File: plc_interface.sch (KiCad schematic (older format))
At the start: 19 parts, among them J501 GPIO, Q601 AO3400A, Q602 AO3401A, U502 PLC_Stamp_mini_2, U601 AMS1117-3.3

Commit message: Add files via upload
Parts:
- removed J501: GPIO, symbol Connector_Generic:Conn_01x04
- added J601: GPIO, Connector_PinSocket_2.54mm:PinSocket_1x06_P2.54mm_Vertical, symbol Connector_Generic:Conn_01x06
- C601, C602: footprint (none) -> Capacitor_SMD:C_0402_1005Metric
- D501, D602: footprint (none) -> LED_SMD:LED_0805_2012Metric
- Q601: footprint (none) -> Package_TO_SOT_SMD:SOT-23
- R501, R502, R503, R504, R505, R508, R510, R606, R607, R609: footprint (none) -> Resistor_SMD:R_0402_1005Metric
- U502: footprint (none) -> PLC stamp:PLC_Stamp_mini_2
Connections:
- wire segments 90 -> 92
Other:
- note added: "Boot Source: Flash"
- note added: "Host Interface: SPI Slave"
- note added: "SPI Slave Mode: Lagacy"
- moved on the sheet: C601, C602, D601, D602, Q601, Q602, R601, R602, R603, R604, R605, R606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

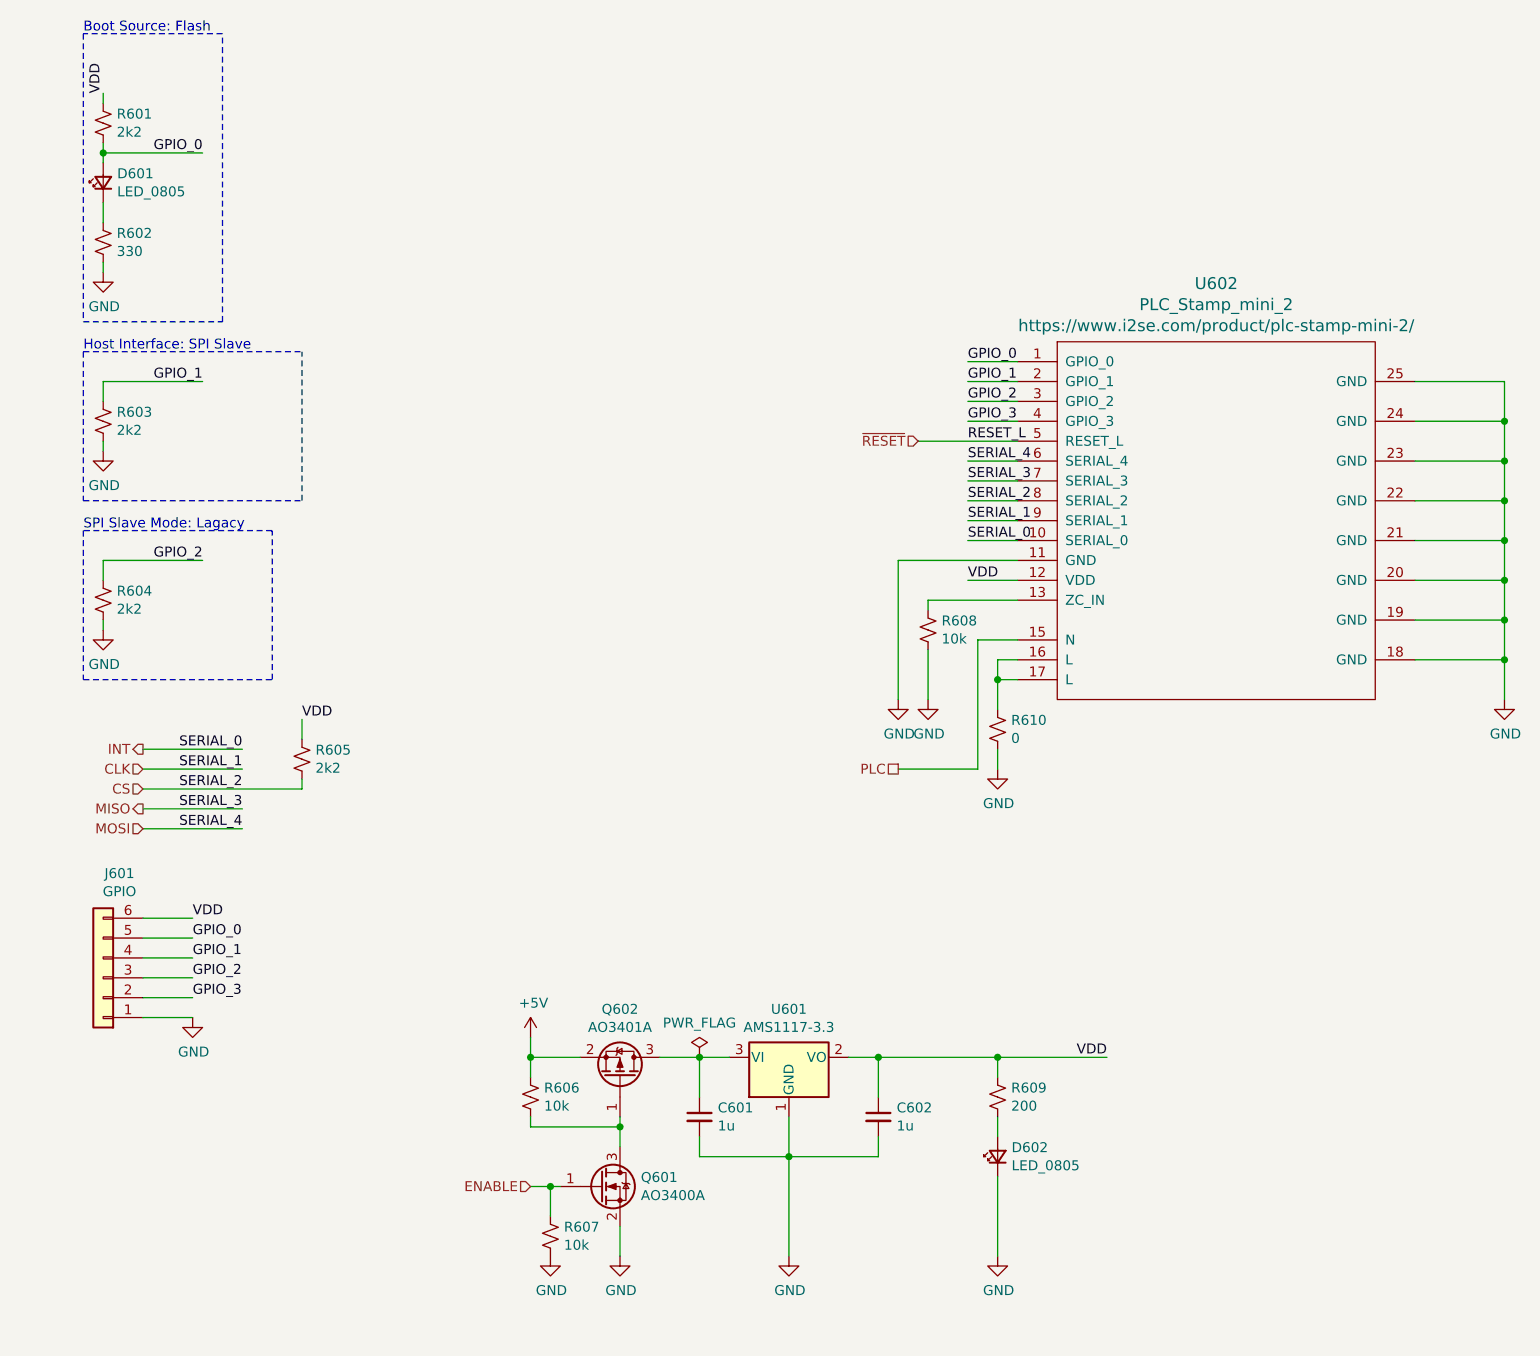
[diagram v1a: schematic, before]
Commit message: Submited for production & smt assembly
v0.01
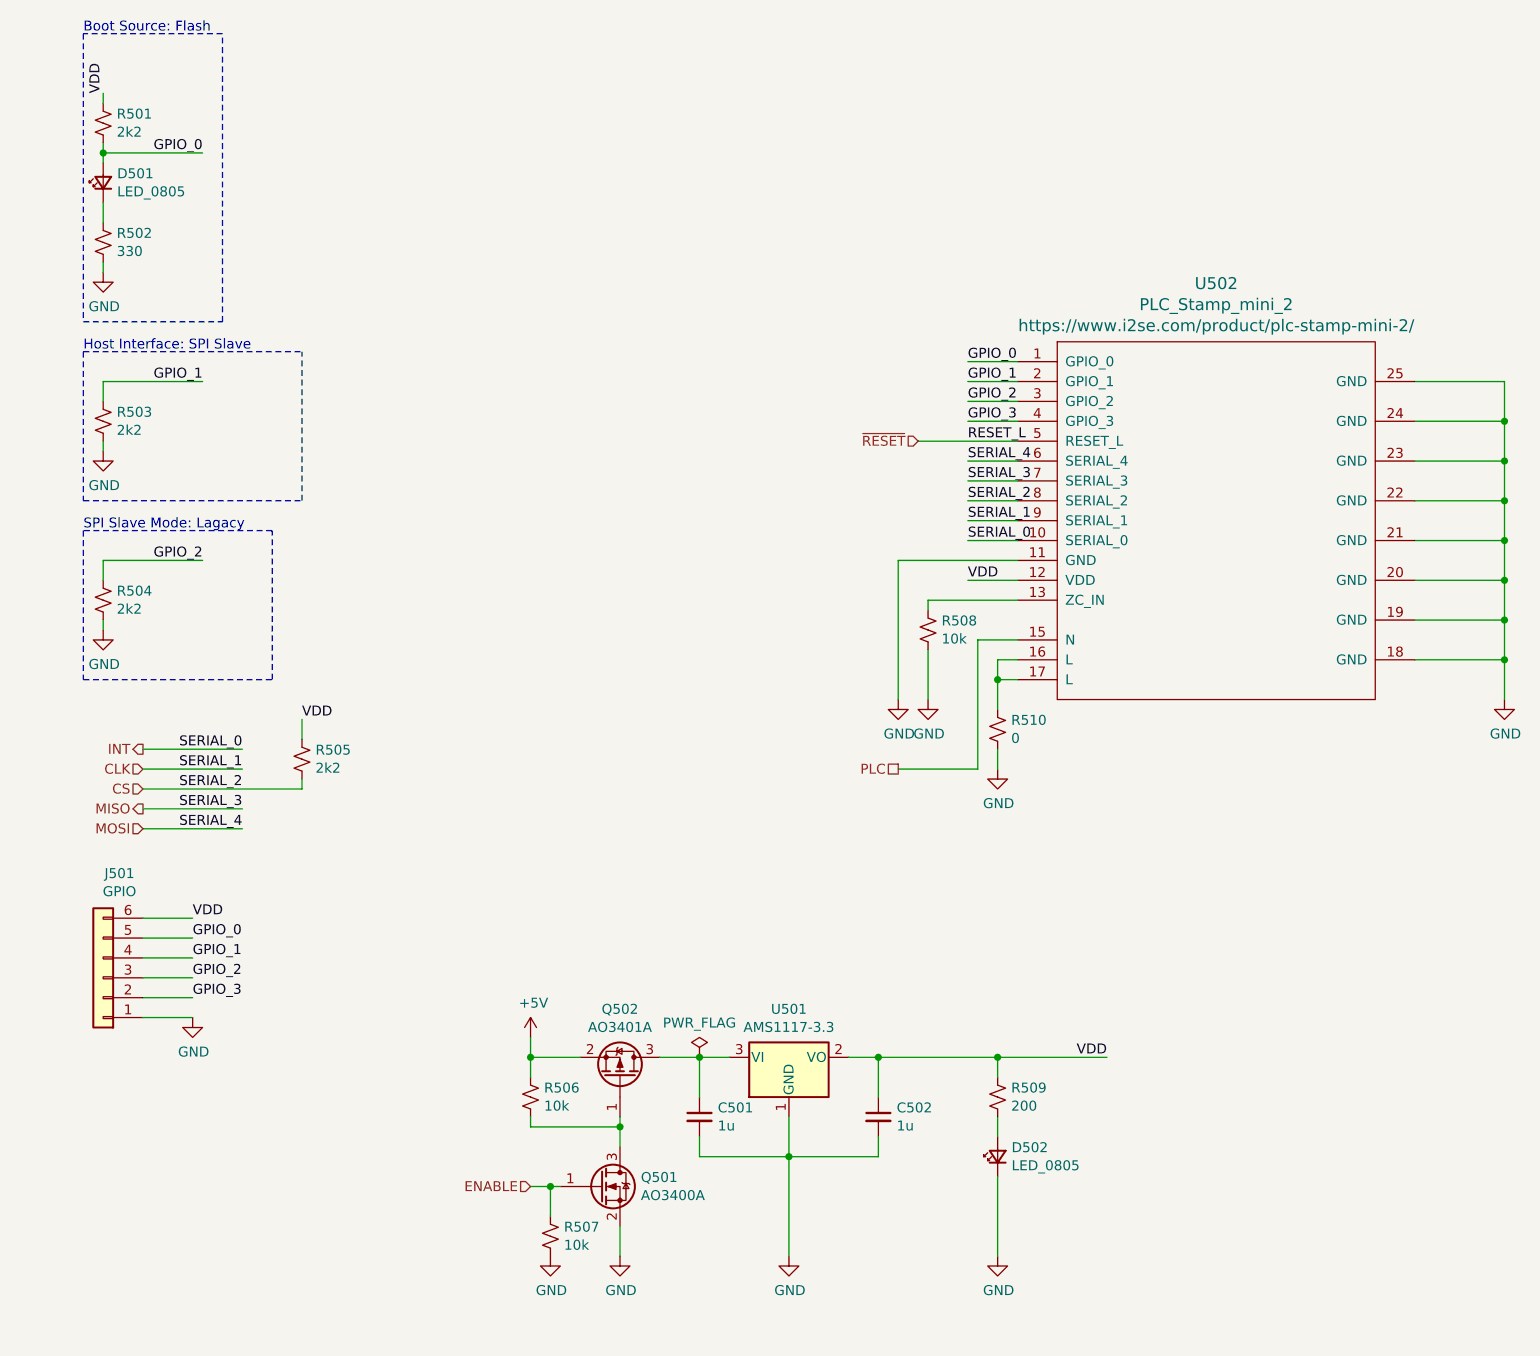
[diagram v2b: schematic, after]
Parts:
- J601: footprint Connector_PinSocket_2.54mm:PinSocket_1x06_P2.54mm_Vertical -> Connector_PinHeader_2.54mm:PinHeader_1x06_P2.54mm_Vertical
- R510: footprint Resistor_SMD:R_0402_1005Metric -> Resistor_SMD:R_0805_2012Metric
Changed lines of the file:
@@
 $Descr A4 11693 8268
 encoding utf-8
-Sheet 6 10
+Sheet 4 10
 Title ""
 Date ""
@@
 AR Path="/5EF2D1B7/5EF2D3AC" Ref="U502"  Part="1"
 AR Path="/5F84D431/5EF2D3AC" Ref="U602"  Part="1"
-F 0 "U602" H 6300 4243 60  0000 C CNN
+F 0 "U502" H 6300 4243 60  0000 C CNN
 F 1 "PLC_Stamp_mini_2" H 6300 4137 60  0000 C CNN
 F 2 "PLC stamp:PLC_Stamp_mini_2" H 6300 3150 60  0001 C CNN
@@
 AR Path="/5EF2D1B7/5EF2EA16" Ref="#PWR0512"  Part="1"
 AR Path="/5F84D431/5EF2EA16" Ref="#PWR0612"  Part="1"
-F 0 "#PWR0612" H 7750 3700 50  0001 C CNN
+F 0 "#PWR0512" H 7750 3700 50  0001 C CNN
 F 1 "GND" H 7755 3777 50  0000 C CNN
 F 2 "" H 7750 3950 50  0001 C CNN
@@
 AR Path="/5EF2D1B7/5EF2FAF1" Ref="R508"  Part="1"
 AR Path="/5F84D431/5EF2FAF1" Ref="R608"  Part="1"
-F 0 "R608" H 4918 3646 50  0000 L CNN
+F 0 "R508" H 4918 3646 50  0000 L CNN
 F 1 "10k" H 4918 3555 50  0000 L CNN
 F 2 "Resistor_SMD:R_0402_1005Metric" H 4850 3600 50  0001 C CNN
@@
 AR Path="/5EF2D1B7/5EF3018B" Ref="#PWR0508"  Part="1"
 AR Path="/5F84D431/5EF3018B" Ref="#PWR0608"  Part="1"
-F 0 "#PWR0608" H 4850 3700 50  0001 C CNN
+F 0 "#PWR0508" H 4850 3700 50  0001 C CNN
 F 1 "GND" H 4855 3777 50  0000 C CNN
 F 2 "" H 4850 3950 50  0001 C CNN
@@
 AR Path="/5EF2D1B7/5EF309BC" Ref="#PWR0507"  Part="1"
 AR Path="/5F84D431/5EF309BC" Ref="#PWR0607"  Part="1"
-F 0 "#PWR0607" H 4700 3700 50  0001 C CNN
+F 0 "#PWR0507" H 4700 3700 50  0001 C CNN
 F 1 "GND" H 4705 3777 50  0000 C CNN
 F 2 "" H 4700 3950 50  0001 C CNN
@@
 AR Path="/5EF2D1B7/5EF3506C" Ref="R501"  Part="1"
 AR Path="/5F84D431/5EF3506C" Ref="R601"  Part="1"
-F 0 "R601" H 768 1096 50  0000 L CNN
+F 0 "R501" H 768 1096 50  0000 L CNN
 F 1 "2k2" H 768 1005 50  0000 L CNN
 F 2 "Resistor_SMD:R_0402_1005Metric" H 700 1050 50  0001 C CNN
@@
 AR Path="/5EF2D1B7/5EF38FDC" Ref="R503"  Part="1"
 AR Path="/5F84D431/5EF38FDC" Ref="R603"  Part="1"
-F 0 "R603" H 768 2596 50  0000 L CNN
+F 0 "R503" H 768 2596 50  0000 L CNN
 F 1 "2k2" H 768 2505 50  0000 L CNN
 F 2 "Resistor_SMD:R_0402_1005Metric" H 700 2550 50  0001 C CNN
@@
 AR Path="/5EF2D1B7/5EF3A4A8" Ref="#PWR0502"  Part="1"
 AR Path="/5F84D431/5EF3A4A8" Ref="#PWR0602"  Part="1"
-F 0 "#PWR0602" H 700 2450 50  0001 C CNN
+F 0 "#PWR0502" H 700 2450 50  0001 C CNN
 F 1 "GND" H 705 2527 50  0000 C CNN
 F 2 "" H 700 2700 50  0001 C CNN
@@
 AR Path="/5EF2D1B7/5EF419EA" Ref="R504"  Part="1"
 AR Path="/5F84D431/5EF419EA" Ref="R604"  Part="1"
-F 0 "R604" H 768 3496 50  0000 L CNN
+F 0 "R504" H 768 3496 50  0000 L CNN
 F 1 "2k2" H 768 3405 50  0000 L CNN
 F 2 "Resistor_SMD:R_0402_1005Metric" H 700 3450 50  0001 C CNN
@@
 AR Path="/5EF2D1B7/5EF41CF1" Ref="#PWR0503"  Part="1"
 AR Path="/5F84D431/5EF41CF1" Ref="#PWR0603"  Part="1"
-F 0 "#PWR0603" H 700 3350 50  0001 C CNN
+F 0 "#PWR0503" H 700 3350 50  0001 C CNN
 F 1 "GND" H 705 3427 50  0000 C CNN
 F 2 "" H 700 3600 50  0001 C CNN
@@
 AR Path="/5EF2D1B7/5EF4D79D" Ref="D501"  Part="1"
 AR Path="/5F84D431/5EF4D79D" Ref="D601"  Part="1"
-F 0 "D601" V 746 1280 50  0000 R CNN
+F 0 "D501" V 746 1280 50  0000 R CNN
 F 1 "LED_0805" V 655 1280 50  0000 R CNN
 F 2 "LED_SMD:LED_0805_2012Metric" V 700 1350 50  0001 C CNN
@@
 AR Path="/5EF2D1B7/5EF4E287" Ref="R502"  Part="1"
 AR Path="/5F84D431/5EF4E287" Ref="R602"  Part="1"
-F 0 "R602" H 768 1696 50  0000 L CNN
+F 0 "R502" H 768 1696 50  0000 L CNN
 F 1 "330" H 768 1605 50  0000 L CNN
 F 2 "Resistor_SMD:R_0402_1005Metric" H 700 1650 50  0001 C CNN
@@
 AR Path="/5EF2D1B7/5EF4E68F" Ref="#PWR0501"  Part="1"
 AR Path="/5F84D431/5EF4E68F" Ref="#PWR0601"  Part="1"
-F 0 "#PWR0601" H 700 1550 50  0001 C CNN
+F 0 "#PWR0501" H 700 1550 50  0001 C CNN
 F 1 "GND" H 705 1627 50  0000 C CNN
 F 2 "" H 700 1800 50  0001 C CNN
@@
 AR Path="/5EF2D1B7/5EF64DDA" Ref="#PWR0509"  Part="1"
 AR Path="/5F84D431/5EF64DDA" Ref="#PWR0609"  Part="1"
-F 0 "#PWR0609" H 5200 4050 50  0001 C CNN
+F 0 "#PWR0509" H 5200 4050 50  0001 C CNN
 F 1 "GND" H 5205 4127 50  0000 C CNN
 F 2 "" H 5200 4300 50  0001 C CNN
@@
 AR Path="/5F84D431/5F90AF35" Ref="U601"  Part="1"
 AR Path="/5EF2D1B7/5F90AF35" Ref="U501"  Part="1"
-F 0 "U601" H 4150 5992 50  0000 C CNN
+F 0 "U501" H 4150 5992 50  0000 C CNN
 F 1 "AMS1117-3.3" H 4150 5901 50  0000 C CNN
 F 2 "Package_TO_SOT_SMD:SOT-223-3_TabPin2" H 4150 5950 50  0001 C CNN
@@
 AR Path="/5F84D431/5F90C7F9" Ref="C601"  Part="1"
 AR Path="/5EF2D1B7/5F90C7F9" Ref="C501"  Part="1"
-F 0 "C601" H 3792 6096 50  0000 L CNN
+F 0 "C501" H 3792 6096 50  0000 L CNN
 F 1 "1u" H 3792 6005 50  0000 L CNN
 F 2 "Capacitor_SMD:C_0402_1005Metric" H 3700 6050 50  0001 C CNN
@@
 AR Path="/5F84D431/5F90CBCB" Ref="C602"  Part="1"
 AR Path="/5EF2D1B7/5F90CBCB" Ref="C502"  Part="1"
-F 0 "C602" H 4692 6096 50  0000 L CNN
+F 0 "C502" H 4692 6096 50  0000 L CNN
 F 1 "1u" H 4692 6005 50  0000 L CNN
 F 2 "Capacitor_SMD:C_0402_1005Metric" H 4600 6050 50  0001 C CNN
@@
 AR Path="/5F84D431/5F90D006" Ref="R609"  Part="1"
 AR Path="/5EF2D1B7/5F90D006" Ref="R509"  Part="1"
-F 0 "R609" H 5268 5996 50  0000 L CNN
+F 0 "R509" H 5268 5996 50  0000 L CNN
 F 1 "200" H 5268 5905 50  0000 L CNN
 F 2 "Resistor_SMD:R_0402_1005Metric" H 5200 5950 50  0001 C CNN
@@
 AR Path="/5F84D431/5F90D610" Ref="D602"  Part="1"
 AR Path="/5EF2D1B7/5F90D610" Ref="D502"  Part="1"
-F 0 "D602" V 5246 6180 50  0000 R CNN
+F 0 "D502" V 5246 6180 50  0000 R CNN
 F 1 "LED_0805" V 5155 6180 50  0000 R CNN
 F 2 "LED_SMD:LED_0805_2012Metric" V 5200 6250 50  0001 C CNN
@@
 AR Path="/5F84D431/5EECEA59" Ref="Q602"  Part="1"
 AR Path="/5EF2D1B7/5EECEA59" Ref="Q502"  Part="1"
-F 0 "Q602" V 3642 5850 50  0000 C CNN
+F 0 "Q502" V 3642 5850 50  0000 C CNN
 F 1 "AO3401A" V 3551 5850 50  0000 C CNN
 F 2 "Package_TO_SOT_SMD:SOT-23" H 3500 5775 50  0001 L CIN
@@
 AR Path="/5F84D431/5EED0EB8" Ref="#PWR0604"  Part="1"
 AR Path="/5EF2D1B7/5EED0EB8" Ref="#PWR0504"  Part="1"
-F 0 "#PWR0604" H 2850 5500 50  0001 C CNN
+F 0 "#PWR0504" H 2850 5500 50  0001 C CNN
 F 1 "+5V" H 2865 5823 50  0000 C CNN
 F 2 "" H 2850 5650 50  0001 C CNN
@@
 AR Path="/5F84D431/5EED1407" Ref="R606"  Part="1"
 AR Path="/5EF2D1B7/5EED1407" Ref="R506"  Part="1"
-F 0 "R606" H 2918 5996 50  0000 L CNN
+F 0 "R506" H 2918 5996 50  0000 L CNN
 F 1 "10k" H 2918 5905 50  0000 L CNN
 F 2 "Resistor_SMD:R_0402_1005Metric" H 2850 5950 50  0001 C CNN
@@
 AR Path="/5F84D431/5EEE7A70" Ref="Q601"  Part="1"
 AR Path="/5EF2D1B7/5EEE7A70" Ref="Q501"  Part="1"
-F 0 "Q601" H 3405 6446 50  0000 L CNN
+F 0 "Q501" H 3405 6446 50  0000 L CNN
 F 1 "AO3400A" H 3405 6355 50  0000 L CNN
 F 2 "Package_TO_SOT_SMD:SOT-23" H 3400 6500 50  0001 C CNN
@@
 AR Path="/5F84D431/5EEE8A1F" Ref="R607"  Part="1"
 AR Path="/5EF2D1B7/5EEE8A1F" Ref="R507"  Part="1"
-F 0 "R607" H 3018 6696 50  0000 L CNN
+F 0 "R507" H 3018 6696 50  0000 L CNN
 F 1 "10k" H 3018 6605 50  0000 L CNN
 F 2 "Resistor_SMD:R_0402_1005Metric" H 2950 6650 50  0001 C CNN
@@
 AR Path="/5F84D431/5EEFA299" Ref="#PWR0605"  Part="1"
 AR Path="/5EF2D1B7/5EEFA299" Ref="#PWR0505"  Part="1"
-F 0 "#PWR0605" H 2950 6500 50  0001 C CNN
+F 0 "#PWR0505" H 2950 6500 50  0001 C CNN
 F 1 "GND" H 2955 6577 50  0000 C CNN
 F 2 "" H 2950 6750 50  0001 C CNN
@@
 AR Path="/5F84D431/5EEFA9B3" Ref="#PWR0606"  Part="1"
 AR Path="/5EF2D1B7/5EEFA9B3" Ref="#PWR0506"  Part="1"
-F 0 "#PWR0606" H 3300 6500 50  0001 C CNN
+F 0 "#PWR0506" H 3300 6500 50  0001 C CNN
 F 1 "GND" H 3305 6577 50  0000 C CNN
 F 2 "" H 3300 6750 50  0001 C CNN
@@
 AR Path="/5F84D431/5EEFABCE" Ref="#PWR0610"  Part="1"
 AR Path="/5EF2D1B7/5EEFABCE" Ref="#PWR0510"  Part="1"
-F 0 "#PWR0610" H 4150 6500 50  0001 C CNN
+F 0 "#PWR0510" H 4150 6500 50  0001 C CNN
 F 1 "GND" H 4155 6577 50  0000 C CNN
 F 2 "" H 4150 6750 50  0001 C CNN
@@
 AR Path="/5F84D431/5EEFAF19" Ref="#PWR0611"  Part="1"
 AR Path="/5EF2D1B7/5EEFAF19" Ref="#PWR0511"  Part="1"
-F 0 "#PWR0611" H 5200 6500 50  0001 C CNN
+F 0 "#PWR0511" H 5200 6500 50  0001 C CNN
 F 1 "GND" H 5205 6577 50  0000 C CNN
 F 2 "" H 5200 6750 50  0001 C CNN
@@
 AR Path="/5EF2D1B7/5F04CB0C" Ref="R505"  Part="1"
 AR Path="/5F84D431/5F04CB0C" Ref="R605"  Part="1"
-F 0 "R605" H 1768 4296 50  0000 L CNN
+F 0 "R505" H 1768 4296 50  0000 L CNN
 F 1 "2k2" H 1768 4205 50  0000 L CNN
 F 2 "Resistor_SMD:R_0402_1005Metric" H 1700 4250 50  0001 C CNN
@@
 AR Path="/5EF2D1B7/5F67AD82" Ref="#FLG0102"  Part="1"
 AR Path="/5F84D431/5F67AD82" Ref="#FLG0103"  Part="1"
-F 0 "#FLG0103" H 3700 5825 50  0001 C CNN
+F 0 "#FLG0102" H 3700 5825 50  0001 C CNN
 F 1 "PWR_FLAG" H 3700 5923 50  0000 C CNN
 F 2 "" H 3700 5750 50  0001 C CNN
@@
 AR Path="/5EF2D1B7/5F681088" Ref="R510"  Part="1"
 AR Path="/5F84D431/5F681088" Ref="R610"  Part="1"
-F 0 "R610" H 5268 4146 50  0000 L CNN
+F 0 "R510" H 5268 4146 50  0000 L CNN
 F 1 "0" H 5268 4055 50  0000 L CNN
-F 2 "Resistor_SMD:R_0402_1005Metric" H 5200 4100 50  0001 C CNN
+F 2 "Resistor_SMD:R_0805_2012Metric" H 5200 4100 50  0001 C CNN
 F 3 "~" H 5200 4100 50  0001 C CNN
 	1    5200 4100
@@
 AR Path="/5F84D431/5EF3A92B" Ref="J601"  Part="1"
 AR Path="/5EF2D1B7/5EF3A92B" Ref="J501"  Part="1"
-F 0 "J601" H 618 4825 50  0000 C CNN
+F 0 "J501" H 618 4825 50  0000 C CNN
 F 1 "GPIO" H 618 4916 50  0000 C CNN
-F 2 "Connector_PinSocket_2.54mm:PinSocket_1x06_P2.54mm_Vertical" H 700 5350 50  0001 C CNN
+F 2 "Connector_PinHeader_2.54mm:PinHeader_1x06_P2.54mm_Vertical" H 700 5350 50  0001 C CNN
 F 3 "~" H 700 5350 50  0001 C CNN
 	1    700  5350
@@
 AR Path="/5EF2D1B7/5EF40C6B" Ref="#PWR0513"  Part="1"
 AR Path="/5F84D431/5EF40C6B" Ref="#PWR0613"  Part="1"
-F 0 "#PWR0613" H 1150 5300 50  0001 C CNN
+F 0 "#PWR0513" H 1150 5300 50  0001 C CNN
 F 1 "GND" H 1155 5377 50  0000 C CNN
 F 2 "" H 1150 5550 50  0001 C CNN
